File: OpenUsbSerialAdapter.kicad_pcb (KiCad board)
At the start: 2 copper layers, 39.8 x 16.4 mm, 21 parts, among them J1 USB_A, J2 FTDI, SW1 SW_DPDT_x2, U1 MCP2200-I-SO, U2 AMS1117-3.3, Y1 12M

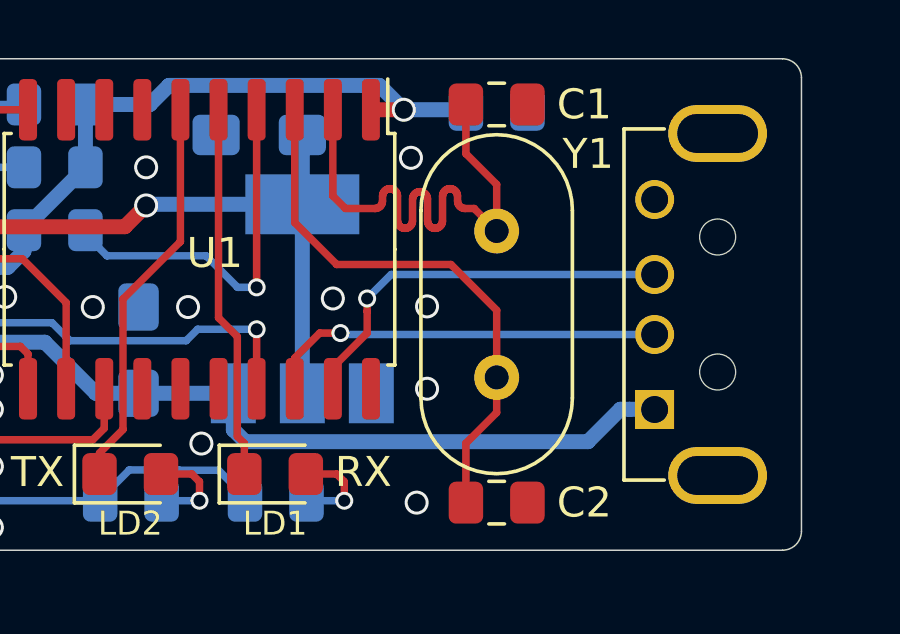
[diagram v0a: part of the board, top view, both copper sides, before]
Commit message: Fix pin order of USB connector, sigh...
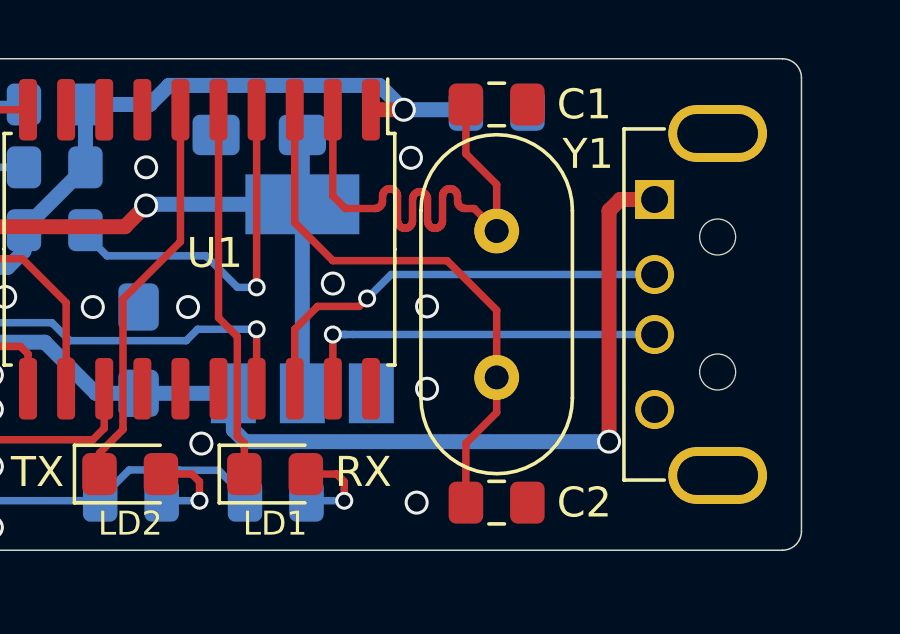
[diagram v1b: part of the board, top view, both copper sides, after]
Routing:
- net +5V: track 29.7 -> 37.1 mm, vias 0 -> 1
- net /usb-: track 13.4 -> 14.7 mm
- net /usb+: track 13.4 -> 12.7 mm
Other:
- board text added: "V2"
- board text removed: "V1"
